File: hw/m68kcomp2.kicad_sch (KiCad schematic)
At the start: 1 part

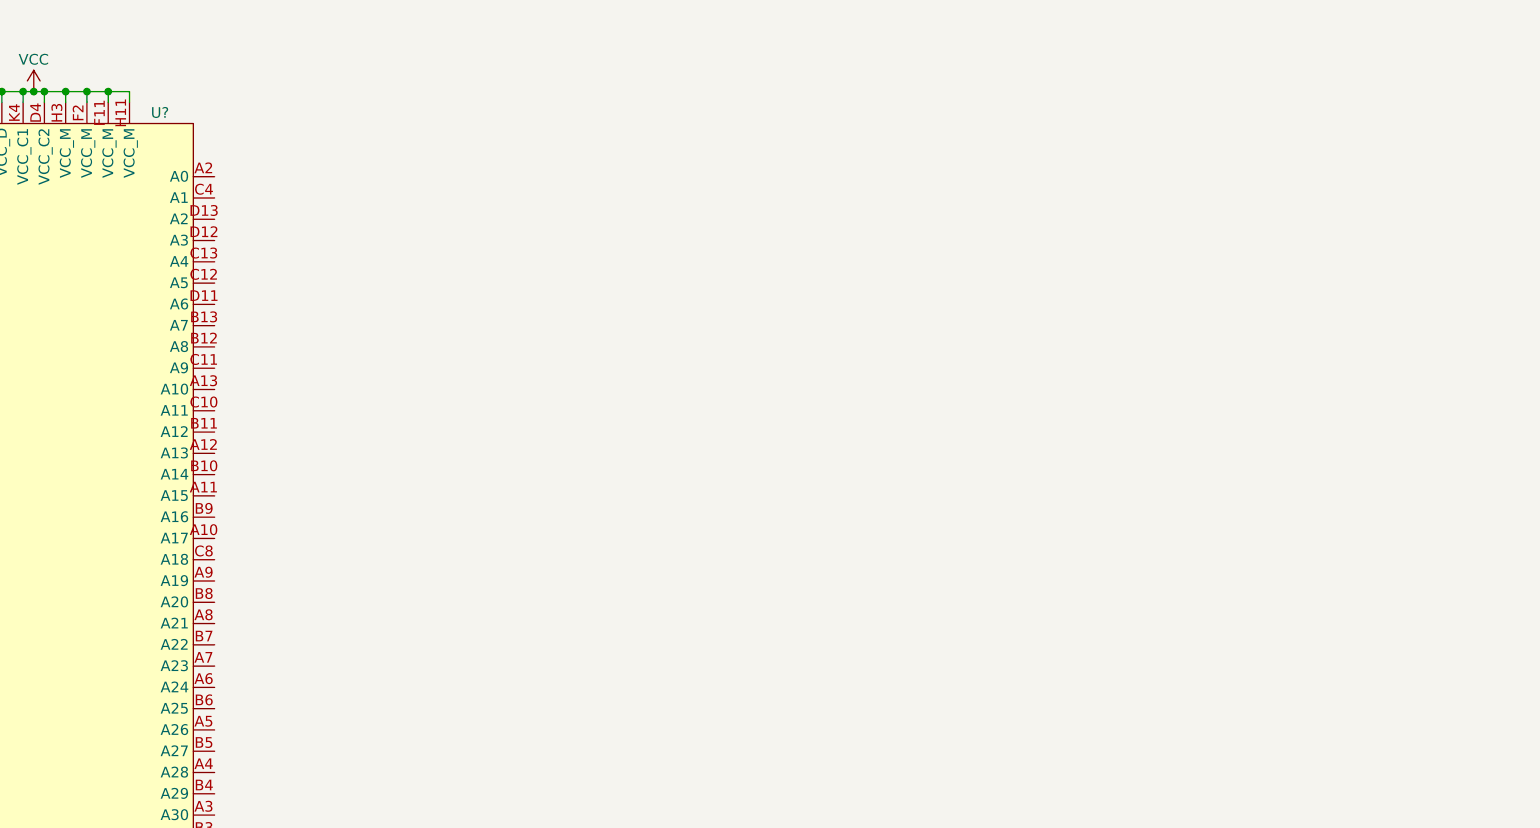
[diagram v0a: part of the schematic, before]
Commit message: added SRAM symbol
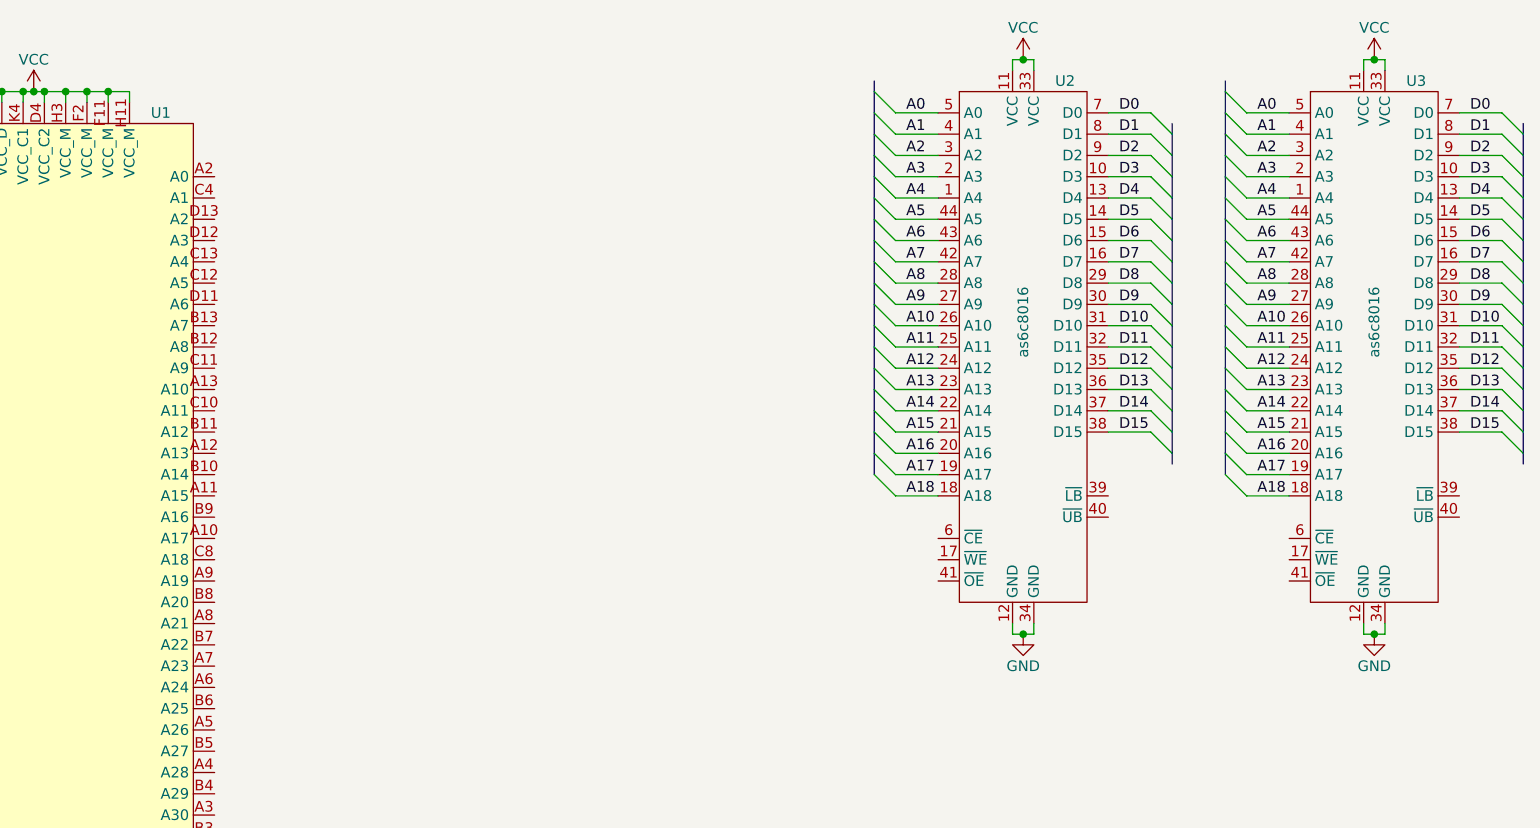
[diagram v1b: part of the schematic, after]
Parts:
- added U2, U3: as6c8016, Package_SO:TSOP-II-44_10.16x18.41mm_P0.8mm, symbol m68kcomp2:as6c8016
- gave numbers to parts that had none: 1
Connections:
- net GND: now also U2.12 (GND), U2.34 (GND), U3.12 (GND), U3.34 (GND)
- net VCC: now also U2.11 (VCC), U2.33 (VCC), U3.11 (VCC), U3.33 (VCC)
- new net A0: U2.5 (A0), U3.5 (A0)
- new net A1: U2.4 (A1), U3.4 (A1)
- new net A10: U2.26 (A10), U3.26 (A10)
- new net A11: U2.25 (A11), U3.25 (A11)
- new net A12: U2.24 (A12), U3.24 (A12)
- new net A13: U2.23 (A13), U3.23 (A13)
- new net A14: U2.22 (A14), U3.22 (A14)
- new net A15: U2.21 (A15), U3.21 (A15)
- new net A16: U2.20 (A16), U3.20 (A16)
- new net A17: U2.19 (A17), U3.19 (A17)
- new net A18: U2.18 (A18), U3.18 (A18)
- new net A2: U2.3 (A2), U3.3 (A2)
- new net A3: U2.2 (A3), U3.2 (A3)
- new net A4: U2.1 (A4), U3.1 (A4)
- new net A5: U2.44 (A5), U3.44 (A5)
- new net A6: U2.43 (A6), U3.43 (A6)
- new net A7: U2.42 (A7), U3.42 (A7)
- new net A8: U2.28 (A8), U3.28 (A8)
- new net A9: U2.27 (A9), U3.27 (A9)
- new net D0: U2.7 (D0), U3.7 (D0)
- new net D1: U2.8 (D1), U3.8 (D1)
- new net D10: U2.31 (D10), U3.31 (D10)
- new net D11: U2.32 (D11), U3.32 (D11)
- new net D12: U2.35 (D12), U3.35 (D12)
- new net D13: U2.36 (D13), U3.36 (D13)
- new net D14: U2.37 (D14), U3.37 (D14)
- new net D15: U2.38 (D15), U3.38 (D15)
- new net D2: U2.9 (D2), U3.9 (D2)
- new net D3: U2.10 (D3), U3.10 (D3)
- new net D4: U2.13 (D4), U3.13 (D4)
- new net D5: U2.14 (D5), U3.14 (D5)
- new net D6: U2.15 (D6), U3.15 (D6)
- new net D7: U2.16 (D7), U3.16 (D7)
- new net D8: U2.29 (D8), U3.29 (D8)
- new net D9: U2.30 (D9), U3.30 (D9)

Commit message: Symbols and rough schematic islands:
  - mc68881 fpu
  - mc68681 duart
  - static ram
  - interrupt priority and acknowledge
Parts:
- removed U2, U3: as6c8016, Package_SO:TSOP-II-44_10.16x18.41mm_P0.8mm, symbol m68kcomp2:as6c8016
- added C? (x2): 12pF, symbol Device:C_Small
- added R?: 4k7, symbol Device:R
- added RN?: 4k7, Resistor_THT:R_Array_SIP9, symbol Device:R_Network08
- added U?: serb, symbol m68kcomp2:rs232_conn
- added U?: sera, symbol m68kcomp2:rs232_conn
- added U?: 28C256, symbol Memory_EEPROM:28C256
- added U? (x4): as6c8008, Package_SO:TSOP-II-44_10.16x18.41mm_P0.8mm, symbol m68kcomp2:as6c8008
- added U?: mc68881, Package_LCC:PLCC-68, symbol m68kcomp2:mc68881
- added U?: 74LS148, symbol 74xx:74LS148
- added U?: GAL16V8, symbol Logic_Programmable:GAL16V8
- added U?: 74LS10, symbol 74xx:74LS10
- added U?: mc68681, symbol m68kcomp2:mc68681
- added U?: mc1489, symbol m68kcomp2:mc1489
- added U? (x2): mc1488, symbol m68kcomp2:mc1488
- added Y?: 3.6864MHz, symbol Device:Crystal_Small
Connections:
- net A0: now also U1.A2 (A0), U?.10 (A0), U?.5 (A0), U?.5 (A0), U?.5 (A0), U?.5 (A0)
- net A1: now also U1.C4 (A1), U?.25 (A1), U?.4 (A1), U?.4 (A1), U?.4 (A1), U?.4 (A1), U?.9 (A1)
- net A10: now also U1.A13 (A10), U?.21 (A10), U?.27 (A10), U?.27 (A10), U?.27 (A10), U?.27 (A10)
- net A11: now also U1.C10 (A11), U?.23 (A11), U?.26 (A11), U?.26 (A11), U?.26 (A11), U?.26 (A11)
- net A12: now also U1.B11 (A12), U?.2 (A12), U?.25 (A12), U?.25 (A12), U?.25 (A12), U?.25 (A12)
- net A13: now also U1.A12 (A13), U?.24 (A13), U?.24 (A13), U?.24 (A13), U?.24 (A13), U?.26 (A13)
- net A14: now also U1.B10 (A14), U?.1 (A14), U?.23 (A14), U?.23 (A14), U?.23 (A14), U?.23 (A14)
- net A15: now also U1.A11 (A15), U?.22 (A15), U?.22 (A15), U?.22 (A15), U?.22 (A15)
- net A16: now also U1.B9 (A16), U?.2 (I2), U?.21 (A16), U?.21 (A16), U?.21 (A16), U?.21 (A16)
- net A17: now also U1.A10 (A17), U?.20 (A17), U?.20 (A17), U?.20 (A17), U?.20 (A17), U?.3 (I3)
- net A18: now also U1.C8 (A18), U?.19 (A18), U?.19 (A18), U?.19 (A18), U?.19 (A18), U?.4 (I4)
- net A2: now also U1.D13 (A2), U?.1 (RS1), U?.24 (A2), U?.3 (A2), U?.3 (A2), U?.3 (A2), U?.3 (A2), U?.8 (A2)
- net A3: now also U1.D12 (A3), U?.2 (A3), U?.2 (A3), U?.2 (A3), U?.2 (A3), U?.23 (A3), U?.3 (RS2), U?.7 (A3)
- net A4: now also U1.C13 (A4), U?.1 (A4), U?.1 (A4), U?.1 (A4), U?.1 (A4), U?.22 (A4), U?.5 (RS3), U?.6 (A4)
- net A5: now also U1.C12 (A5), U?.44 (A5), U?.44 (A5), U?.44 (A5), U?.44 (A5), U?.5 (A5), U?.6 (RS4)
- net A6: now also U1.D11 (A6), U?.4 (A6), U?.43 (A6), U?.43 (A6), U?.43 (A6), U?.43 (A6)
- net A7: now also U1.B13 (A7), U?.3 (A7), U?.42 (A7), U?.42 (A7), U?.42 (A7), U?.42 (A7)
- net A8: now also U1.B12 (A8), U?.25 (A8), U?.39 (A8), U?.39 (A8), U?.39 (A8), U?.39 (A8)
- net A9: now also U1.C11 (A9), U?.24 (A9), U?.28 (A9), U?.28 (A9), U?.28 (A9), U?.28 (A9)
- net D0: now also U1.K13 (D0), U?.11 (D0), U?.25 (D0), U?.3 (D0), U?.9 (D0)
- net D1: now also U1.K12 (D1), U?.10 (D1), U?.12 (D1), U?.16 (D1), U?.2 (D1)
- net D10: now also U1.L10 (D10), U?.13 (D2), U?.59 (D10)
- net D11: now also U1.N12 (D11), U?.14 (D3), U?.58 (D11)
- net D12: now also U1.M10 (D12), U?.31 (D4), U?.57 (D12)
- net D13: now also U1.N11 (D13), U?.32 (D5), U?.56 (D13)
- net D14: now also U1.M9 (D14), U?.35 (D6), U?.55 (D14)
- net D15: now also U1.N10 (D15), U?.36 (D7), U?.54 (D15)
- net D2: now also U1.L13 (D2), U?.1 (D2), U?.13 (D2), U?.13 (D2), U?.24 (D2)
- net D3: now also U1.M13 (D3), U?.14 (D3), U?.15 (D3), U?.17 (D3), U?.68 (D3)
- net D4: now also U1.L12 (D4), U?.16 (D4), U?.23 (D4), U?.31 (D4), U?.67 (D4)
- net D5: now also U1.K11 (D5), U?.17 (D5), U?.18 (D5), U?.32 (D5), U?.66 (D5)
- net D6: now also U1.M12 (D6), U?.18 (D6), U?.22 (D6), U?.35 (D6), U?.65 (D6)
- net D7: now also U1.L11 (D7), U?.19 (D7), U?.19 (D7), U?.36 (D7), U?.64 (D7)
- net D8: now also U1.N13 (D8), U?.62 (D8), U?.9 (D0)
- net D9: now also U1.M11 (D9), U?.10 (D1), U?.60 (D9)
- net GND: now also C?.2, C?.2, U?.10 (3B), U?.10 (GND), U?.12 (4A), U?.12 (GND), U?.12 (GND), U?.12 (GND), U?.12 (GND), U?.12 (GND), U?.13 (4B), U?.14 (GND), U?.14 (GND), U?.19 (GND), U?.2 (IP3), U?.20 (GND), U?.30 (GND), U?.34 (GND), U?.34 (GND), U?.34 (GND), U?.34 (GND), U?.36 (IP2), U?.38 (IP5), U?.39 (IP4), U?.41 (GND), U?.5 (EI), U?.5 (GND), U?.51 (GND), U?.6 (GND), U?.63 (GND), U?.7 (GND), U?.7 (GND), U?.7 (GND), U?.7 (GND), U?.8 (GND), U?.8 (GND), U?.9 (3A), U?.9 (GND), U?.GND (5), U?.GND (5)
- net VCC: now also R?.1, RN?.1 (common), U?.10 (IO), U?.10 (VCC), U?.11 (VCC), U?.11 (VCC), U?.11 (VCC), U?.11 (VCC), U?.14 (VCC), U?.16 (VCC), U?.16 (VCC), U?.17 (VCC), U?.18 (~{SIZE}), U?.20 (VCC), U?.26 (A0), U?.27 (VCC), U?.28 (VCC), U?.33 (VCC), U?.33 (VCC), U?.33 (VCC), U?.33 (VCC), U?.40 (VCC), U?.43 (VCC), U?.52 (VCC), U?.53 (VCC), U?.61 (VCC)
- net A30: now reaches U1.A3 (A30)
- net A28: now reaches U1.A4 (A28)
- net A26: now reaches U1.A5 (A26)
- net A24: now reaches U1.A6 (A24)
- net A23: now reaches U1.A7 (A23)
- net A21: now reaches U1.A8 (A21)
- net A19: now reaches U1.A9 (A19)
- net A19: now also U?.18 (A19), U?.18 (A19), U?.18 (A19), U?.18 (A19), U?.5 (I5)
- net A31: now reaches U1.B3 (A31)
- net A29: now reaches U1.B4 (A29)
- net A27: now reaches U1.B5 (A27)
- net A25: now reaches U1.B6 (A25)
- net A22: now reaches U1.B7 (A22)
- net A20: now reaches U1.B8 (A20)
- net FC1: now reaches U1.C1 (FC1)
- net FC1: now also U?.2
- net FC2: now reaches U1.D1 (FC2)
- net FC2: now also U?.1
- net FC0: now reaches U1.D2 (FC0)
- net FC0: now also U?.13
- net CPUCLK: now reaches U1.E1 (CLK)
- net ~{AVEC}: now reaches U1.E2 (~{AVEC})
- net at U1.G12 (~{IPL2}): now also U?.6 (S2)
- net at U1.G13 (~{IPL1}): now also U?.7 (S1)
- net at U1.H13 (~{IPL0}): now also U?.9 (S0)
- net D30: now reaches U1.L4 (D30)
- net D30: now also U?.34 (D30), U?.35 (D6)
- net D29: now reaches U1.M3 (D29)
- net D29: now also U?.32 (D5), U?.35 (D29)
- net D27: now reaches U1.M4 (D27)
- net D27: now also U?.14 (D3), U?.37 (D27)
- net D24: now reaches U1.M5 (D24)
- net D24: now also U?.40 (D24), U?.9 (D0)
- net D22: now reaches U1.M6 (D22)
- net D22: now also U?.35 (D6), U?.44 (D22)
- net D20: now reaches U1.M7 (D20)
- net D20: now also U?.31 (D4), U?.46 (D20)
- net D17: now reaches U1.M8 (D17)
- net D17: now also U?.10 (D1), U?.49 (D17)
- net D31: now reaches U1.N1 (D31)
- net D31: now also U?.33 (D31), U?.36 (D7)
- net D28: now reaches U1.N2 (D28)
- net D28: now also U?.31 (D4), U?.36 (D28)
- net D26: now reaches U1.N3 (D26)
- net D26: now also U?.13 (D2), U?.38 (D26)
- net D25: now reaches U1.N4 (D25)
- net D25: now also U?.10 (D1), U?.39 (D25)
- net D23: now reaches U1.N5 (D23)
- net D23: now also U?.36 (D7), U?.42 (D23)
- net D21: now reaches U1.N6 (D21)
- net D21: now also U?.32 (D5), U?.45 (D21)
- net D19: now reaches U1.N7 (D19)
- net D19: now also U?.14 (D3), U?.47 (D19)
- net D18: now reaches U1.N8 (D18)
- net D18: now also U?.13 (D2), U?.48 (D18)
- net D16: now reaches U1.N9 (D16)
- net D16: now also U?.50 (D16), U?.9 (D0)
- new net: C?.1, U?.32 (X1/CLK), Y?.1
- new net: C?.1, U?.33 (X2), Y?.2
- new net +12V: U?.14 (V+), U?.14 (V+)
- new net -12V: U?.1 (V-), U?.1 (V-)
- new net CTSA: U?.6 (2Y), U?.7 (IP0)
- new net CTSA_232: U?.4 (2A), U?.CTS (8)
- new net CTSB: U?.11 (4Y), U?.4 (IP1)
- new net CTSB_232: U?.13 (4A), U?.CTS (8)
- new net DTRA: U?.2 (1A), U?.27 (OP4)
- new net DTRA_232: U?.3 (1Y), U?.DTR (4)
- new net DTRB: U?.14 (OP5), U?.4 (2A), U?.5 (2B)
- new net DTRB_232: U?.6 (2Y), U?.DTR (4)
- new net FPUCLK: U?.11 (CLK)
- new net FPUEN: U?.29 (~{CS})
- new net RTRA: U?.29 (OP0), U?.4 (2A), U?.5 (2B)
- new net RTRA_232: U?.6 (2Y), U?.RTS (7)
- new net RTRB: U?.12 (4A), U?.12 (OP1)
- new net RTRB_232: U?.11 (4Y), U?.RTS (7)
- new net RXDA: U?.3 (1Y), U?.31 (RxDA)
- new net RXDA_232: U?.1 (1A), U?.RXD (2)
- new net RXDB: U?.10 (RxDB), U?.8 (3Y)
- new net RXDB_232: U?.10 (3A), U?.RXD (2)
- new net R/~{W}: U?.28 (R/~{W})
- new net TXDA: U?.2 (1A), U?.30 (TxDA)
- new net TXDA_232: U?.3 (1Y), U?.TXD (3)
- new net TXDB: U?.11 (TxDB), U?.9 (3A)
- new net TXDB_232: U?.8 (3Y), U?.TXD (3)
- new net ~{AS}: U?.21 (~{AS}), U?.9 (I9)
- new net ~{DSACK0}: U?.31 (~{DSACK0})
- new net ~{DSACK1}: U?.32 (~{DSACK1})
- new net ~{DS}: U?.20 (~{DS})
- new net ~{FCPU}: U?.1 (I1/CLK), U?.12
- new net ~{FPU}: R?.2, U?.4 (~{SENSE})
- new net ~{IACK}: U?.19 (IO1)
- new net ~{IRQ0}: RN?.2 (R1), U?.11 (I1)
- new net ~{IRQ1}: RN?.3 (R2), U?.12 (I2)
- new net ~{IRQ2}: RN?.4 (R3), U?.13 (I3)
- new net ~{IRQ3}: RN?.5 (R4), U?.1 (I4)
- new net ~{IRQ4}: RN?.6 (R5), U?.2 (I5)
- new net ~{IRQ5}: RN?.7 (R6), U?.3 (I6)
- new net ~{NMI}: RN?.8 (R7), U?.4 (I7)
- new net ~{RAMEN}: U?.17 (I03)
- new net ~{RESET}: U?.13 (~{RESET}), U?.34 (~{RESET})
- new net ~{ROMEN}: U?.18 (IO2)
- no-connect marks 0 -> 19
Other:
- note added: "IACK = ~{FCPU} * ~{AS} * A16 * A17 * A18 * A19"
- moved on the sheet: U1

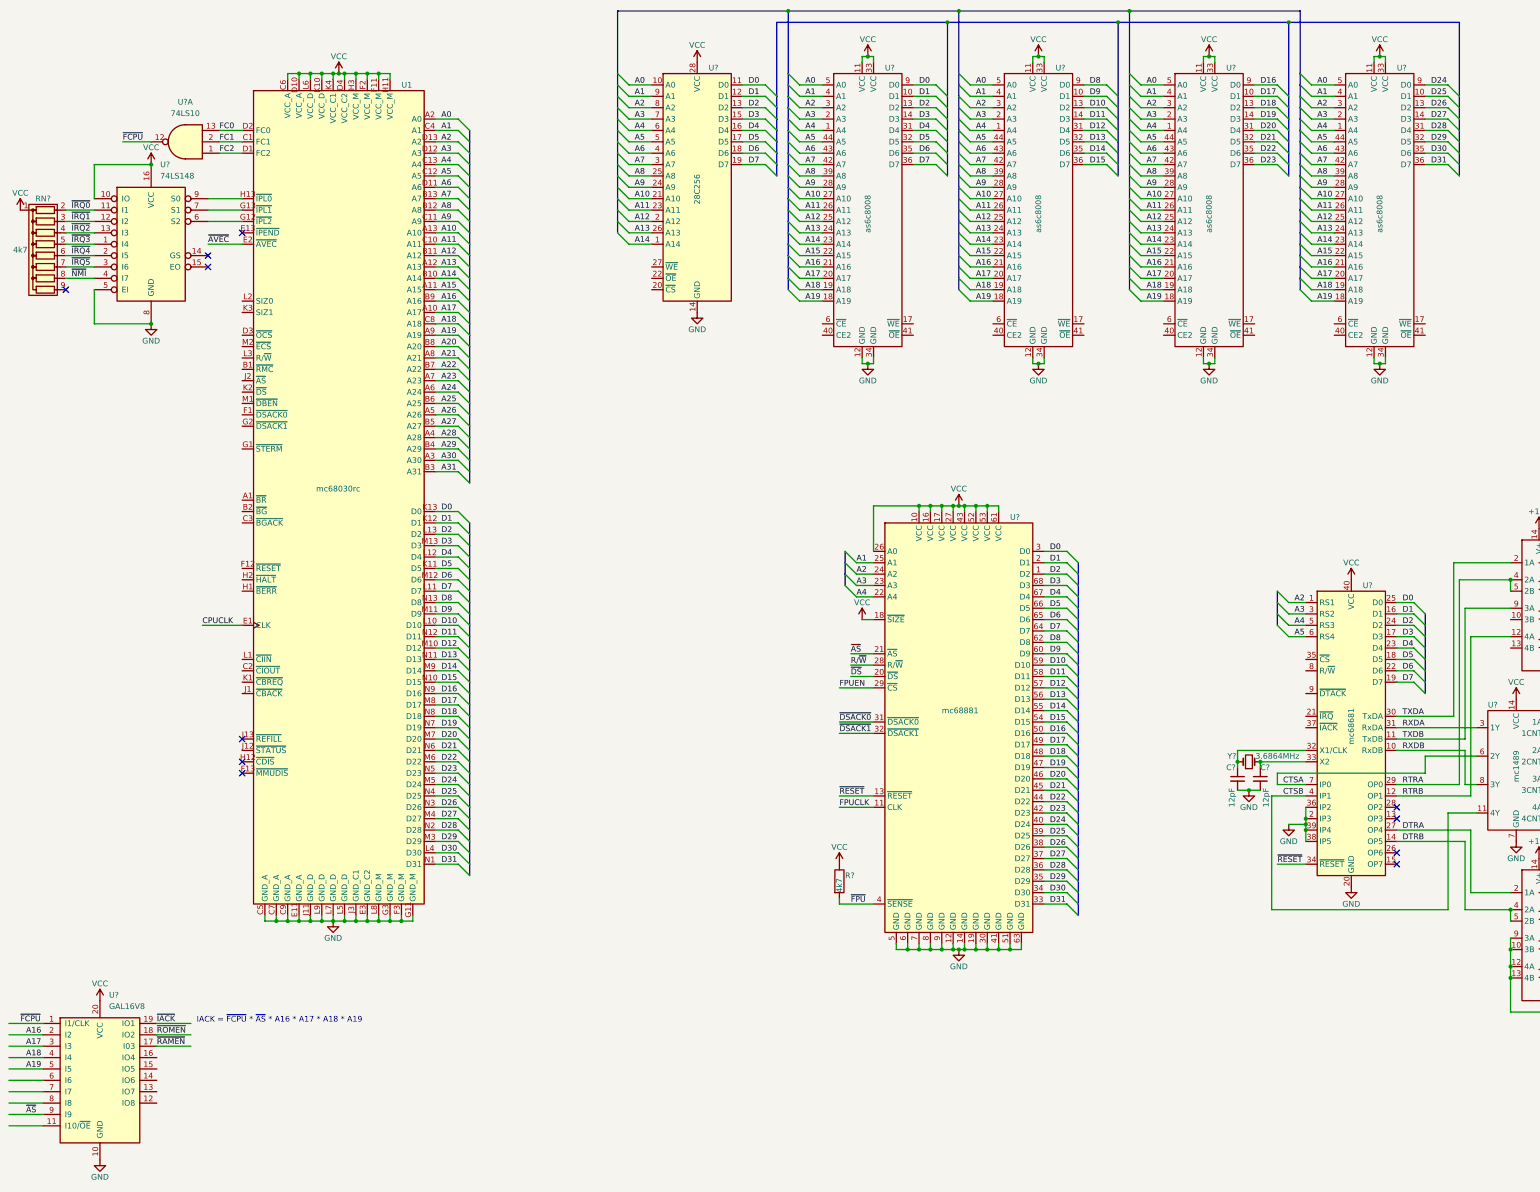
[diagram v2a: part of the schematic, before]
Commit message: address decoding
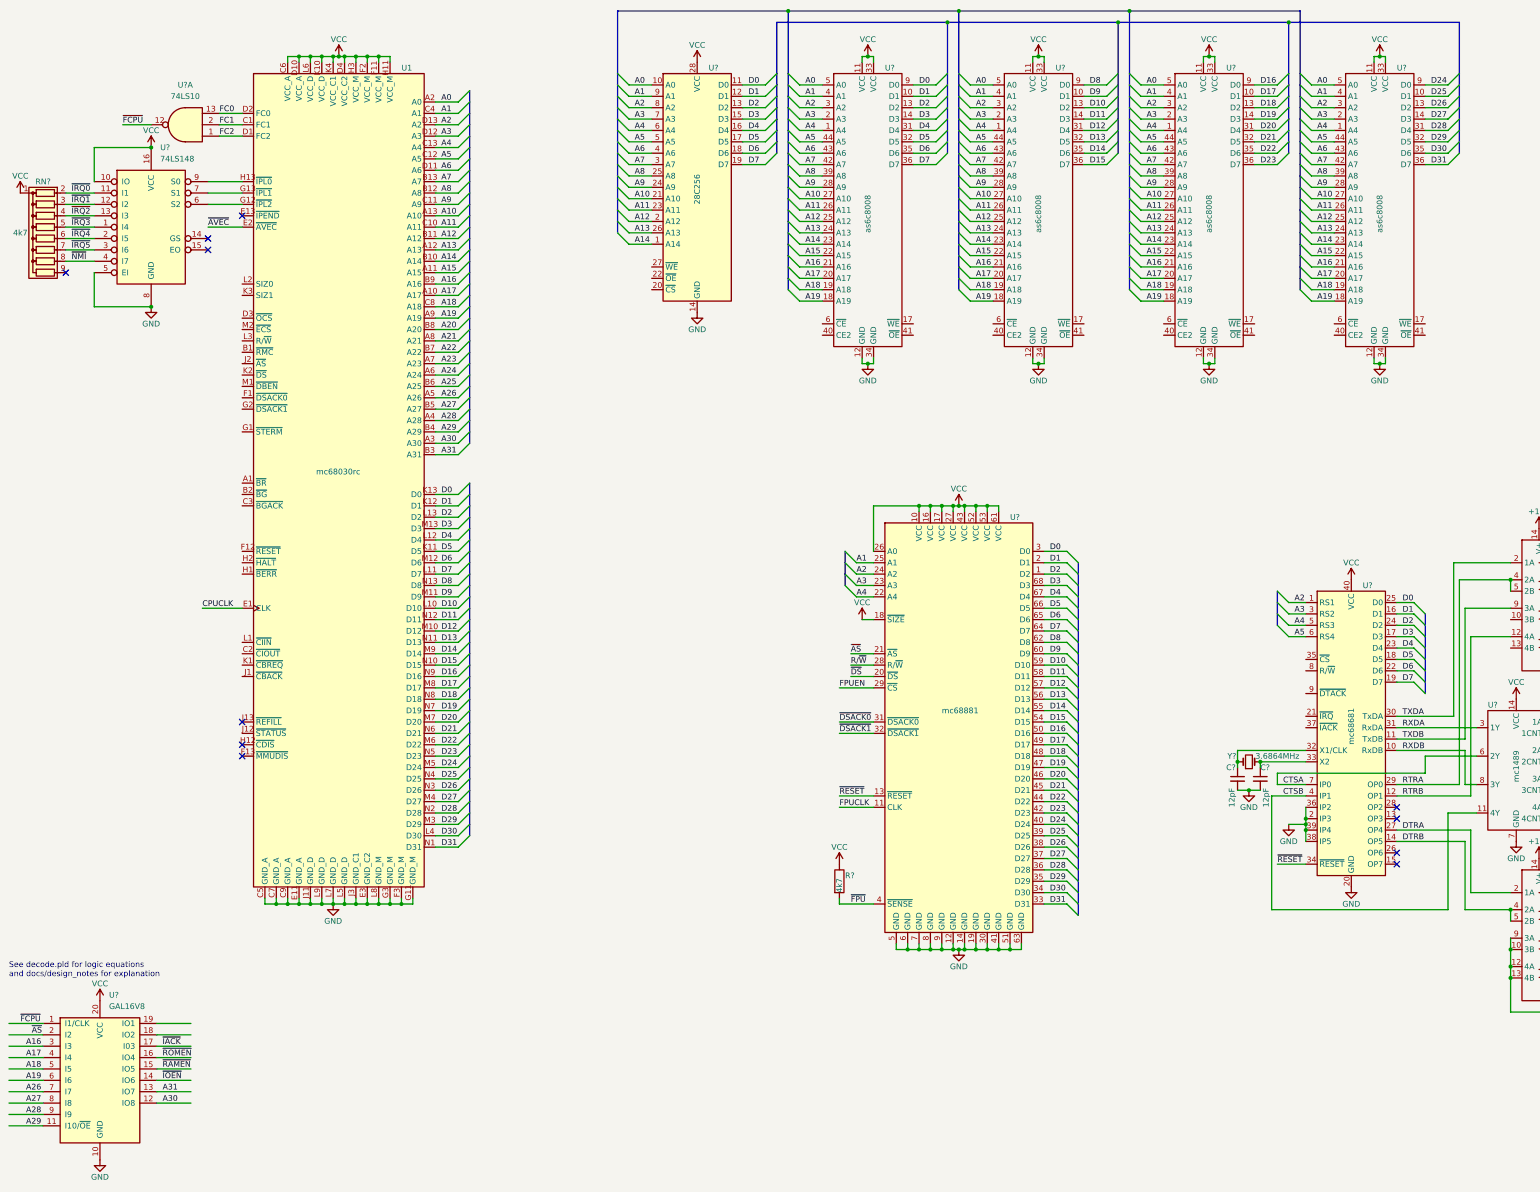
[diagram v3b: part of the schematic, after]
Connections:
- net A16: now also U?.3 (I3); no longer U?.2 (I2)
- net A17: now also U?.4 (I4); no longer U?.3 (I3)
- net A18: now also U?.5 (I5); no longer U?.4 (I4)
- net A19: now also U?.6 (I6); no longer U?.5 (I5)
- net A26: now also U?.7 (I7)
- net A27: now also U?.8 (I8)
- net A28: now also U?.9 (I9)
- net A29: now also U?.11 (I10/~{OE})
- net A30: now also U?.12 (IO8)
- net A31: now also U?.13 (IO7)
- net ~{AS}: now also U?.2 (I2); no longer U?.9 (I9)
- net ~{IACK}: now also U?.17 (I03); no longer U?.19 (IO1)
- net ~{RAMEN}: now also U?.15 (IO5); no longer U?.17 (I03)
- net ~{ROMEN}: now also U?.16 (IO4); no longer U?.18 (IO2)
- net ~{IOEN}: now reaches U?.14 (IO6)
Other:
- note added: "See decode.pld for logic equations and docs/design_notes for explanation"
- note removed: "IACK = ~{FCPU} * ~{AS} * A16 * A17 * A18 * A19"
- moved on the sheet: RN?, U1, U?, U?A
